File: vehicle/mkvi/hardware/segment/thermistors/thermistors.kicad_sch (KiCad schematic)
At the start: 1 part, among them J1 Microfit_VT_16

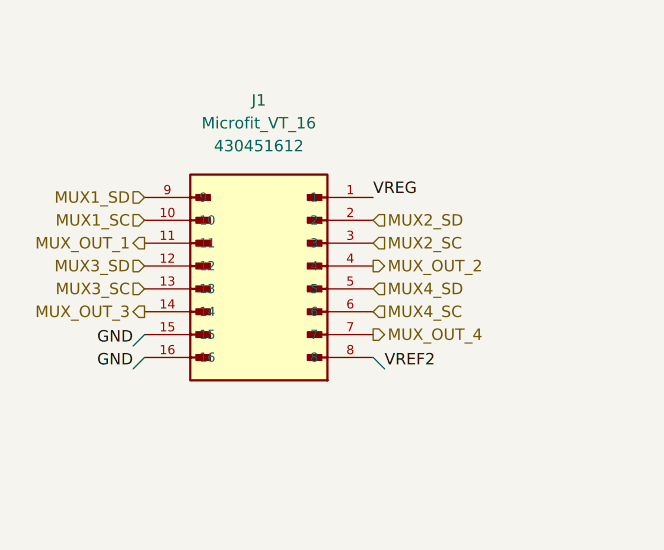
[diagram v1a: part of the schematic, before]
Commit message: final mux routing
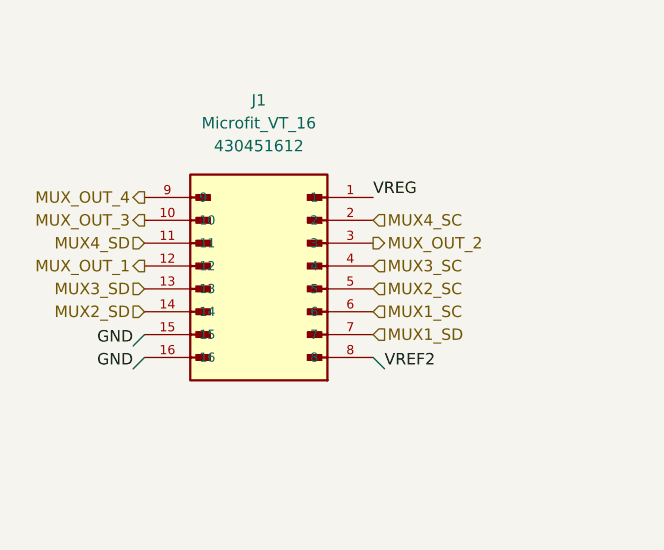
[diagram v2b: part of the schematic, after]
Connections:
- net MUX1_SC: now also J1.6; no longer J1.10
- net MUX1_SD: now also J1.7; no longer J1.9
- net MUX2_SC: now also J1.5; no longer J1.3
- net MUX2_SD: now also J1.14; no longer J1.2
- net MUX3_SC: now also J1.4; no longer J1.13
- net MUX3_SD: now also J1.13; no longer J1.12
- net MUX4_SC: now also J1.2; no longer J1.6
- net MUX4_SD: now also J1.11; no longer J1.5
- net MUX_OUT_1: now also J1.12; no longer J1.11
- net MUX_OUT_2: now also J1.3; no longer J1.4
- net MUX_OUT_3: now also J1.10; no longer J1.14
- net MUX_OUT_4: now also J1.9; no longer J1.7
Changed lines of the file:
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@@
     (effects (font (size 1.27 1.27)) (justify left))
   )
-  (hierarchical_label "MUX_OUT_3" (shape output) (at 39.37 48.895 180)
+  (hierarchical_label "MUX_OUT_3" (shape output) (at 39.37 38.735 180)
     (effects (font (size 1.27 1.27)) (justify right))
   )
@@
     (effects (font (size 1.27 1.27)) (justify left))
   )
-  (hierarchical_label "MUX3_SC" (shape input) (at 39.37 46.355 180)
-    (effects (font (size 1.27 1.27)) (justify right))
+  (hierarchical_label "MUX3_SC" (shape input) (at 64.77 43.815 0)
+    (effects (font (size 1.27 1.27)) (justify left))
   )
-  (hierarchical_label "MUX3_SD" (shape input) (at 39.37 43.815 180)
+  (hierarchical_label "MUX3_SD" (shape input) (at 39.37 46.355 180)
     (effects (font (size 1.27 1.27)) (justify right))
   )
@@
     (effects (font (size 1.27 1.27)) (justify left))
   )
-  (hierarchical_label "MUX1_SD" (shape input) (at 39.37 36.195 180)
-    (effects (font (size 1.27 1.27)) (justify right))
-  )
-  (hierarchical_label "MUX4_SC" (shape input) (at 64.77 48.895 0)
+  (hierarchical_label "MUX1_SD" (shape input) (at 64.77 51.435 0)
     (effects (font (size 1.27 1.27)) (justify left))
   )
-  (hierarchical_label "MUX2_SD" (shape input) (at 64.77 38.735 0)
+  (hierarchical_label "MUX4_SC" (shape input) (at 64.77 38.735 0)
     (effects (font (size 1.27 1.27)) (justify left))
+  )
+  (hierarchical_label "MUX2_SD" (shape input) (at 39.37 48.895 180)
+    (effects (font (size 1.27 1.27)) (justify right))
   )
   (hierarchical_label "MUX3_SD" (shape input) (at 235.585 100.965 0)
@@
     (effects (font (size 1.27 1.27)) (justify left))
   )
-  (hierarchical_label "MUX_OUT_1" (shape output) (at 39.37 41.275 180)
+  (hierarchical_label "MUX_OUT_1" (shape output) (at 39.37 43.815 180)
     (effects (font (size 1.27 1.27)) (justify right))
   )
@@
     (effects (font (size 1.27 1.27)) (justify left))
   )
-  (hierarchical_label "MUX4_SD" (shape input) (at 64.77 46.355 0)
-    (effects (font (size 1.27 1.27)) (justify left))
+  (hierarchical_label "MUX4_SD" (shape input) (at 39.37 41.275 180)
+    (effects (font (size 1.27 1.27)) (justify right))
   )
   (hierarchical_label "MUX_OUT_1" (shape output) (at 234.315 34.925 0)
@@
     (effects (font (size 1.27 1.27)) (justify left))
   )
-  (hierarchical_label "MUX1_SC" (shape input) (at 39.37 38.735 180)
-    (effects (font (size 1.27 1.27)) (justify right))
-  )
-  (hierarchical_label "MUX_OUT_2" (shape output) (at 64.77 43.815 0)
+  (hierarchical_label "MUX1_SC" (shape input) (at 64.77 48.895 0)
     (effects (font (size 1.27 1.27)) (justify left))
   )
-  (hierarchical_label "MUX_OUT_4" (shape output) (at 64.77 51.435 0)
+  (hierarchical_label "MUX_OUT_2" (shape output) (at 64.77 41.275 0)
     (effects (font (size 1.27 1.27)) (justify left))
+  )
+  (hierarchical_label "MUX_OUT_4" (shape output) (at 39.37 36.195 180)
+    (effects (font (size 1.27 1.27)) (justify right))
   )
   (hierarchical_label "MUX1_SC" (shape input) (at 234.315 31.115 0)
     (effects (font (size 1.27 1.27)) (justify left))
   )
-  (hierarchical_label "MUX2_SC" (shape input) (at 64.77 41.275 0)
+  (hierarchical_label "MUX2_SC" (shape input) (at 64.77 46.355 0)
     (effects (font (size 1.27 1.27)) (justify left))
   )

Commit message: boards ready for review
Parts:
- removed J1: Microfit_VT_16, OEM:Microfit_VT_16, symbol OEM:Microfit_VT_16
- added J1: TST-108-01-T-D, OEM:TST-108-XX-T-D, symbol OEM:TST-108-01-T-D
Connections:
- net GND: now also J1.2, J1.4
- net MUX1_SC: now also J1.5
- net MUX1_SD: now also J1.3
- net MUX2_SC: now also J1.7
- net MUX2_SD: now also J1.6
- net MUX3_SC: now also J1.9
- net MUX3_SD: now also J1.8
- net MUX4_SC: now also J1.13
- net MUX4_SD: now also J1.12
- net MUX_OUT_1: now also J1.14
- net MUX_OUT_2: now also J1.10
- net MUX_OUT_3: now also J1.16
- net MUX_OUT_4: now also J1.11
- net VREF2: now also J1.1
- net VREG: now also J1.15
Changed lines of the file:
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@@
 (kicad_sch (version 20211123) (generator eeschema)
   (paper "A4")
-  (wire (pts (xy 38.1 52.705) (xy 39.37 51.435))
-    (stroke (width 0) (type default) (color 0 0 0 0))
-  )
-  (wire (pts (xy 66.04 55.245) (xy 64.77 53.975))
+  (wire (pts (xy 64.135 62.23) (xy 62.865 63.5))
+    (stroke (width 0) (type default) (color 0 0 0 0))
+  )
+  (wire (pts (xy 38.735 59.69) (xy 40.005 60.96))
     (stroke (width 0) (type default) (color 0 0 0 0))
   )
@@
     (stroke (width 0) (type default) (color 0 0 0 0))
   )
-  (wire (pts (xy 38.1 55.245) (xy 39.37 53.975))
+  (wire (pts (xy 64.135 59.69) (xy 62.865 60.96))
     (stroke (width 0) (type default) (color 0 0 0 0))
   )
@@
     (effects (font (size 1.27 1.27)) (justify right bottom))
   )
-  (label "VREG" (at 64.77 36.195 0)
-    (effects (font (size 1.27 1.27)) (justify left bottom))
+  (label "VREG" (at 40.005 78.74 180)
+    (effects (font (size 1.27 1.27)) (justify right bottom))
   )
   (label "GND" (at 153.67 154.94 270)
@@
     (effects (font (size 1.27 1.27)) (justify right bottom))
   )
-  (label "VREF2" (at 66.04 55.245 0)
-    (effects (font (size 1.27 1.27)) (justify left bottom))
+  (label "VREF2" (at 38.735 59.69 180)
+    (effects (font (size 1.27 1.27)) (justify right bottom))
   )
   (label "VREG" (at 211.455 58.42 90)
@@
     (effects (font (size 1.27 1.27)) (justify left bottom))
   )
-  (label "GND" (at 38.1 55.245 180)
-    (effects (font (size 1.27 1.27)) (justify right bottom))
+  (label "GND" (at 64.135 59.69 0)
+    (effects (font (size 1.27 1.27)) (justify left bottom))
   )
   (label "VREF2" (at 234.315 38.735 0)
@@
     (effects (font (size 1.27 1.27)) (justify right bottom))
   )
-  (label "GND" (at 38.1 52.705 180)
-    (effects (font (size 1.27 1.27)) (justify right bottom))
+  (label "GND" (at 64.135 62.23 0)
+    (effects (font (size 1.27 1.27)) (justify left bottom))
   )
   (label "VREG" (at 211.455 22.225 90)
@@
     (effects (font (size 1.27 1.27)) (justify left))
   )
-  (hierarchical_label "MUX_OUT_3" (shape output) (at 39.37 38.735 180)
-    (effects (font (size 1.27 1.27)) (justify right))
+  (hierarchical_label "MUX_OUT_3" (shape output) (at 62.865 78.74 0)
+    (effects (font (size 1.27 1.27)) (justify left))
   )
   (hierarchical_label "MUX4_SC" (shape input) (at 235.585 140.335 0)
     (effects (font (size 1.27 1.27)) (justify left))
   )
-  (hierarchical_label "MUX3_SC" (shape input) (at 64.77 43.815 0)
-    (effects (font (size 1.27 1.27)) (justify left))
-  )
-  (hierarchical_label "MUX3_SD" (shape input) (at 39.37 46.355 180)
-    (effects (font (size 1.27 1.27)) (justify right))
+  (hierarchical_label "MUX3_SC" (shape input) (at 40.005 71.12 180)
+    (effects (font (size 1.27 1.27)) (justify right))
+  )
+  (hierarchical_label "MUX3_SD" (shape input) (at 62.865 68.58 0)
+    (effects (font (size 1.27 1.27)) (justify left))
   )
   (hierarchical_label "MUX4_SD" (shape input) (at 235.585 136.525 0)
     (effects (font (size 1.27 1.27)) (justify left))
   )
-  (hierarchical_label "MUX1_SD" (shape input) (at 64.77 51.435 0)
-    (effects (font (size 1.27 1.27)) (justify left))
-  )
-  (hierarchical_label "MUX4_SC" (shape input) (at 64.77 38.735 0)
-    (effects (font (size 1.27 1.27)) (justify left))
-  )
-  (hierarchical_label "MUX2_SD" (shape input) (at 39.37 48.895 180)
-    (effects (font (size 1.27 1.27)) (justify right))
+  (hierarchical_label "MUX1_SD" (shape input) (at 40.005 63.5 180)
+    (effects (font (size 1.27 1.27)) (justify right))
+  )
+  (hierarchical_label "MUX4_SC" (shape input) (at 40.005 76.2 180)
+    (effects (font (size 1.27 1.27)) (justify right))
+  )
+  (hierarchical_label "MUX2_SD" (shape input) (at 62.865 66.04 0)
+    (effects (font (size 1.27 1.27)) (justify left))
   )
   (hierarchical_label "MUX3_SD" (shape input) (at 235.585 100.965 0)
@@
     (effects (font (size 1.27 1.27)) (justify left))
   )
-  (hierarchical_label "MUX_OUT_1" (shape output) (at 39.37 43.815 180)
-    (effects (font (size 1.27 1.27)) (justify right))
+  (hierarchical_label "MUX_OUT_1" (shape output) (at 62.865 76.2 0)
+    (effects (font (size 1.27 1.27)) (justify left))
   )
   (hierarchical_label "MUX2_SD" (shape input) (at 234.315 63.5 0)
     (effects (font (size 1.27 1.27)) (justify left))
   )
-  (hierarchical_label "MUX4_SD" (shape input) (at 39.37 41.275 180)
-    (effects (font (size 1.27 1.27)) (justify right))
+  (hierarchical_label "MUX4_SD" (shape input) (at 62.865 73.66 0)
+    (effects (font (size 1.27 1.27)) (justify left))
   )
   (hierarchical_label "MUX_OUT_1" (shape output) (at 234.315 34.925 0)
@@
     (effects (font (size 1.27 1.27)) (justify left))
   )
-  (hierarchical_label "MUX1_SC" (shape input) (at 64.77 48.895 0)
-    (effects (font (size 1.27 1.27)) (justify left))
-  )
-  (hierarchical_label "MUX_OUT_2" (shape output) (at 64.77 41.275 0)
-    (effects (font (size 1.27 1.27)) (justify left))
-  )
-  (hierarchical_label "MUX_OUT_4" (shape output) (at 39.37 36.195 180)
+  (hierarchical_label "MUX1_SC" (shape input) (at 40.005 66.04 180)
+    (effects (font (size 1.27 1.27)) (justify right))
+  )
+  (hierarchical_label "MUX_OUT_2" (shape output) (at 62.865 71.12 0)
+    (effects (font (size 1.27 1.27)) (justify left))
+  )
+  (hierarchical_label "MUX_OUT_4" (shape output) (at 40.005 73.66 180)
     (effects (font (size 1.27 1.27)) (justify right))
   )
@@
     (effects (font (size 1.27 1.27)) (justify left))
   )
-  (hierarchical_label "MUX2_SC" (shape input) (at 64.77 46.355 0)
-    (effects (font (size 1.27 1.27)) (justify left))
+  (hierarchical_label "MUX2_SC" (shape input) (at 40.005 68.58 180)
+    (effects (font (size 1.27 1.27)) (justify right))
   )
   (hierarchical_label "MUX1_SD" (shape input) (at 234.315 27.305 0)
     (effects (font (size 1.27 1.27)) (justify left))
   )
-  (symbol (lib_id "OEM:Microfit_VT_16") (at 52.07 46.355 0) (mirror y) (unit 1)
+  (symbol (lib_id "OEM:TST-108-01-T-D") (at 51.435 69.85 0) (unit 1)
     (in_bom yes) (on_board yes) (fields_autoplaced)
-    (property "Reference" "J1" (id 0) (at 52.07 25.4 0))
-    (property "Value" "Microfit_VT_16" (id 1) (at 52.07 27.94 0))
-    (property "Footprint" "OEM:Microfit_VT_16" (id 2) (at 52.07 46.355 0)
-      (effects (font (size 1.27 1.27)) (justify bottom) hide)
-    )
-    (property "Datasheet" "" (id 3) (at 52.07 46.355 0)
-      (effects (font (size 1.27 1.27)) hide)
-    )
-    (property "MPN" "430451612" (id 4) (at 52.07 30.48 0))
+    (property "Reference" "J1" (id 0) (at 51.435 86.36 0))
+    (property "Value" "TST-108-01-T-D" (id 1) (at 51.435 83.82 0))
+    (property "Footprint" "OEM:TST-108-XX-T-D" (id 2) (at 59.055 58.42 0)
+      (effects (font (size 1.27 1.27)) (justify left) hide)
+    )
+    (property "Datasheet" "http://suddendocs.samtec.com/prints/tst-1xx-xx-x-x-xx-xx-mkt.pdf" (id 3) (at 70.485 69.85 0)
+      (effects (font (size 1.27 1.27)) (justify left) hide)
+    )
+    (property "MPN" "TST-108-01-T-D" (id 4) (at 59.055 76.2 0)
+      (effects (font (size 1.27 1.27)) (justify left) hide)
+    )
     (pin "1")
     (pin "10")
@@
   )
   (symbol_instances
-    (path "/029042a6-cd6e-4c5f-9a5f-19e8bc5b0145"
-      (reference "J1") (unit 1) (value "Microfit_VT_16") (footprint "OEM:Microfit_VT_16")
+    (path "/7ec9e0f6-5422-44a9-9017-f820289c7b87"
+      (reference "J1") (unit 1) (value "TST-108-01-T-D") (footprint "OEM:TST-108-XX-T-D")
     )
     (path "/efc2f6a0-556c-4b46-86f0-4a7c2d3fd33b/46f84645-04a0-4dac-a596-19e31ff52ac7"

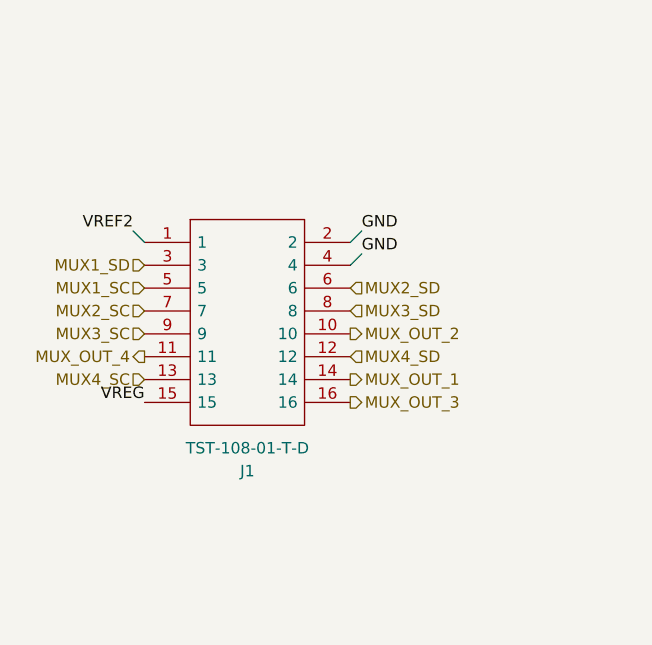
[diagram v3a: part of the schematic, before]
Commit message: move connectors to resolve clearance issue
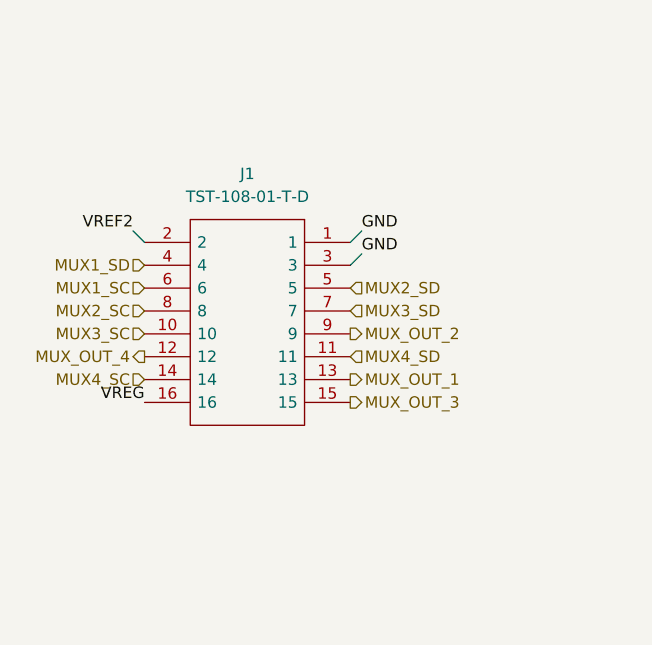
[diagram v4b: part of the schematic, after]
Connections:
- net GND: now also J1.1, J1.3; no longer J1.2, J1.4
- net MUX1_SC: now also J1.6; no longer J1.5
- net MUX1_SD: now also J1.4; no longer J1.3
- net MUX2_SC: now also J1.8; no longer J1.7
- net MUX2_SD: now also J1.5; no longer J1.6
- net MUX3_SC: now also J1.10; no longer J1.9
- net MUX3_SD: now also J1.7; no longer J1.8
- net MUX4_SC: now also J1.14; no longer J1.13
- net MUX4_SD: now also J1.11; no longer J1.12
- net MUX_OUT_1: now also J1.13; no longer J1.14
- net MUX_OUT_2: now also J1.9; no longer J1.10
- net MUX_OUT_3: now also J1.15; no longer J1.16
- net MUX_OUT_4: now also J1.12; no longer J1.11
- net VREF2: now also J1.2; no longer J1.1
- net VREG: now also J1.16; no longer J1.15
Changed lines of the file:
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@@
     (effects (font (size 1.27 1.27)) (justify left))
   )
-  (symbol (lib_id "OEM:TST-108-01-T-D") (at 51.435 69.85 0) (unit 1)
+  (symbol (lib_id "OEM:TST-108-01-T-D") (at 51.435 69.85 0) (mirror y) (unit 1)
     (in_bom yes) (on_board yes) (fields_autoplaced)
-    (property "Reference" "J1" (id 0) (at 51.435 86.36 0))
-    (property "Value" "TST-108-01-T-D" (id 1) (at 51.435 83.82 0))
-    (property "Footprint" "OEM:TST-108-XX-T-D" (id 2) (at 59.055 58.42 0)
+    (property "Reference" "J1" (id 0) (at 51.435 53.34 0))
+    (property "Value" "TST-108-01-T-D" (id 1) (at 51.435 55.88 0))
+    (property "Footprint" "OEM:TST-108-XX-T-D" (id 2) (at 43.815 58.42 0)
       (effects (font (size 1.27 1.27)) (justify left) hide)
     )
-    (property "Datasheet" "http://suddendocs.samtec.com/prints/tst-1xx-xx-x-x-xx-xx-mkt.pdf" (id 3) (at 70.485 69.85 0)
+    (property "Datasheet" "http://suddendocs.samtec.com/prints/tst-1xx-xx-x-x-xx-xx-mkt.pdf" (id 3) (at 32.385 69.85 0)
       (effects (font (size 1.27 1.27)) (justify left) hide)
     )
-    (property "MPN" "TST-108-01-T-D" (id 4) (at 59.055 76.2 0)
+    (property "MPN" "TST-108-01-T-D" (id 4) (at 43.815 76.2 0)
       (effects (font (size 1.27 1.27)) (justify left) hide)
     )
